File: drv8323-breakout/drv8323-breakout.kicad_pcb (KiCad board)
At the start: 2 copper layers, 49.8 x 40 mm, 43 parts, among them J1 Conn_01x02_Pin, J2 Conn_01x04_Pin, J3 Screw_Terminal_01x03, J4 Conn_01x03_Pin, J5 Screw_Terminal_01x02, J6 Screw_Terminal_01x02, J7 Conn_02x03_Odd_Even, U1 DRV8323HRTAR, U2 CSD18534Q5A, U3 CSD18534Q5A, U4 CSD18534Q5A, U5 CSD18534Q5A, U6 CSD18534Q5A, U7 CSD18534Q5A

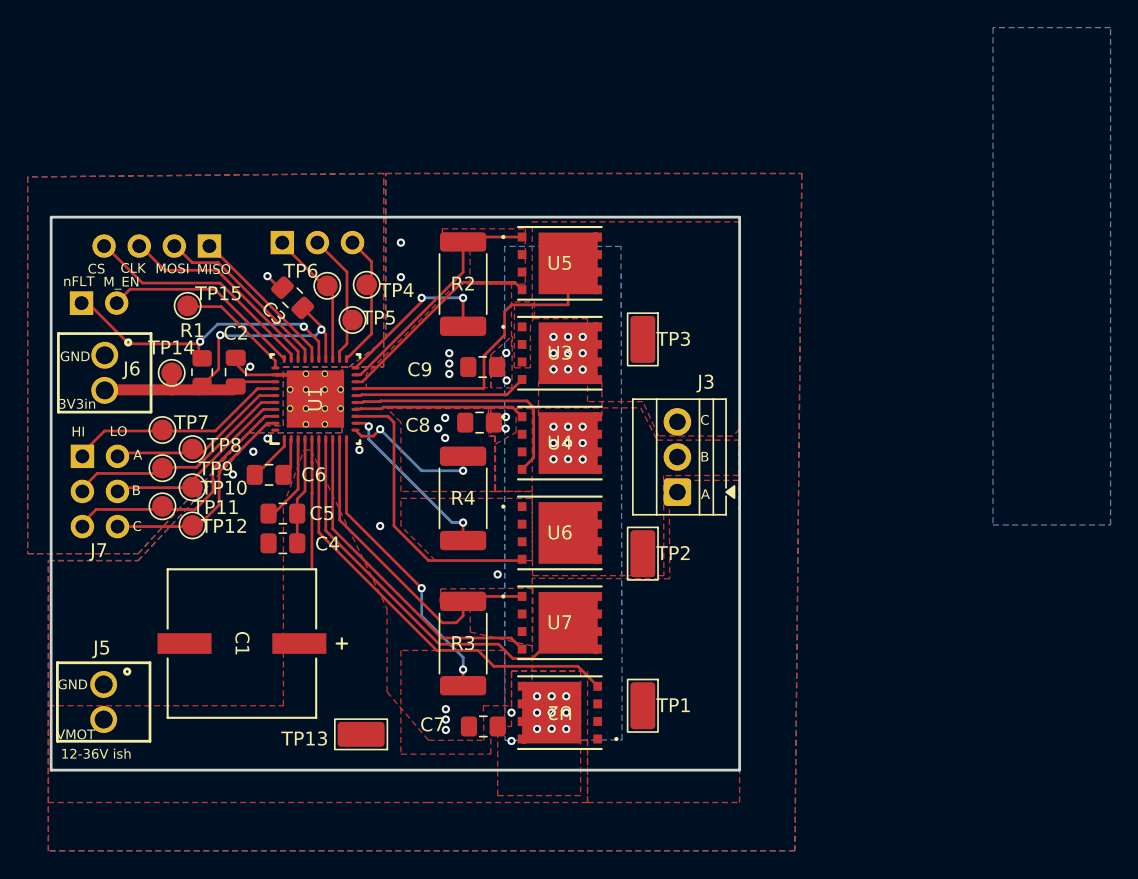
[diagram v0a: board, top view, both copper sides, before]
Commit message: updated symbols for sanity and PCB for mfg, no DRC errors, only net type ERC errors
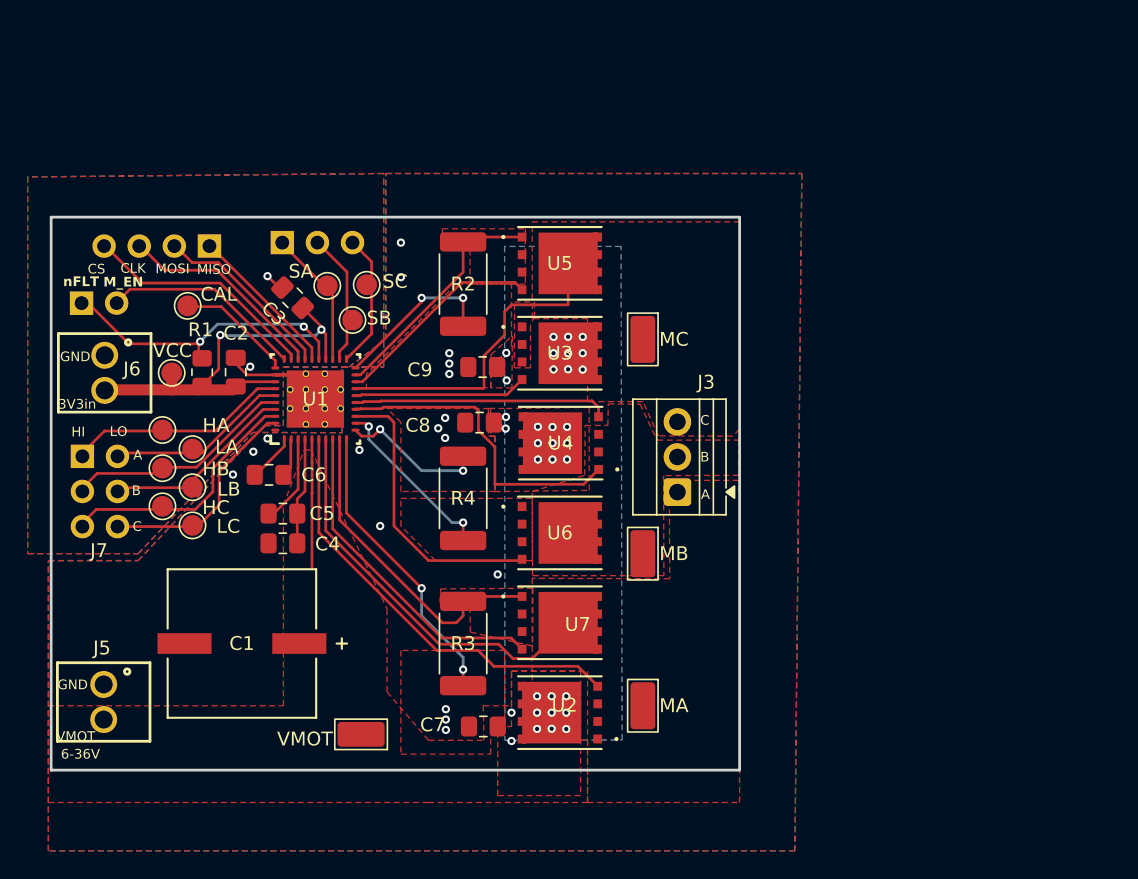
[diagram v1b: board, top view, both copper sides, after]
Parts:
- moved U4 0.06 mm to (136.1, 74.5), turned to 180 degrees
- renumbered TP15 to CAL, TP7 to HA, TP9 to HB, TP11 to HC, TP8 to LA, TP10 to LB, TP12 to LC, TP1 to MA, TP2 to MB, TP3 to MC, TP6 to SA, TP5 to SB, TP4 to SC, TP14 to VCC, TP13 to VMOT
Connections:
- R2 pad 2: /Motor Control/SNC -> PGND
- R3 pad 2: /Motor Control/SNA -> PGND
- R4 pad 2: /Motor Control/SNB -> PGND
- U1 pad 10: /Motor Control/SNA -> PGND
- U1 pad 11: /Motor Control/SNB -> PGND
- U1 pad 20: /Motor Control/SNC -> PGND
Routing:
- net PGND: track 0.00 -> 42.8 mm, vias 17 -> 23
- net /Motor Control/SNA: track 21.3 -> 0.00 mm, vias 2 -> 0
- net /Motor Control/SNC: track 12.1 -> 0.00 mm, vias 2 -> 0
- net MOT_B: track 12.4 -> 22.8 mm
- net /Motor Control/SNB: track 9.42 -> 0.00 mm, vias 2 -> 0
- net V_MOT: track 19.3 -> 18.2 mm
- net Net-(U1-GHB): track 18.0 -> 18.5 mm
- removed copper zone on F.Cu, net /Motor Control/SNA
- removed copper zone on F.Cu, net /Motor Control/SNB
- removed copper zone on F.Cu, net /Motor Control/SNC
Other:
- board text added: "6-36V"
- board text removed: "12-36V ish"
